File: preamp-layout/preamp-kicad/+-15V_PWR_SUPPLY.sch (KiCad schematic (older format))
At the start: 33 parts, among them J5 Screw_Terminal_01x03, J6 Conn_01x03_Male, J7 Conn_01x03_Male, J8 Conn_01x03_Male, T1 Transformer_1P_2S, U1 L7805, U2 LM7905_TO220

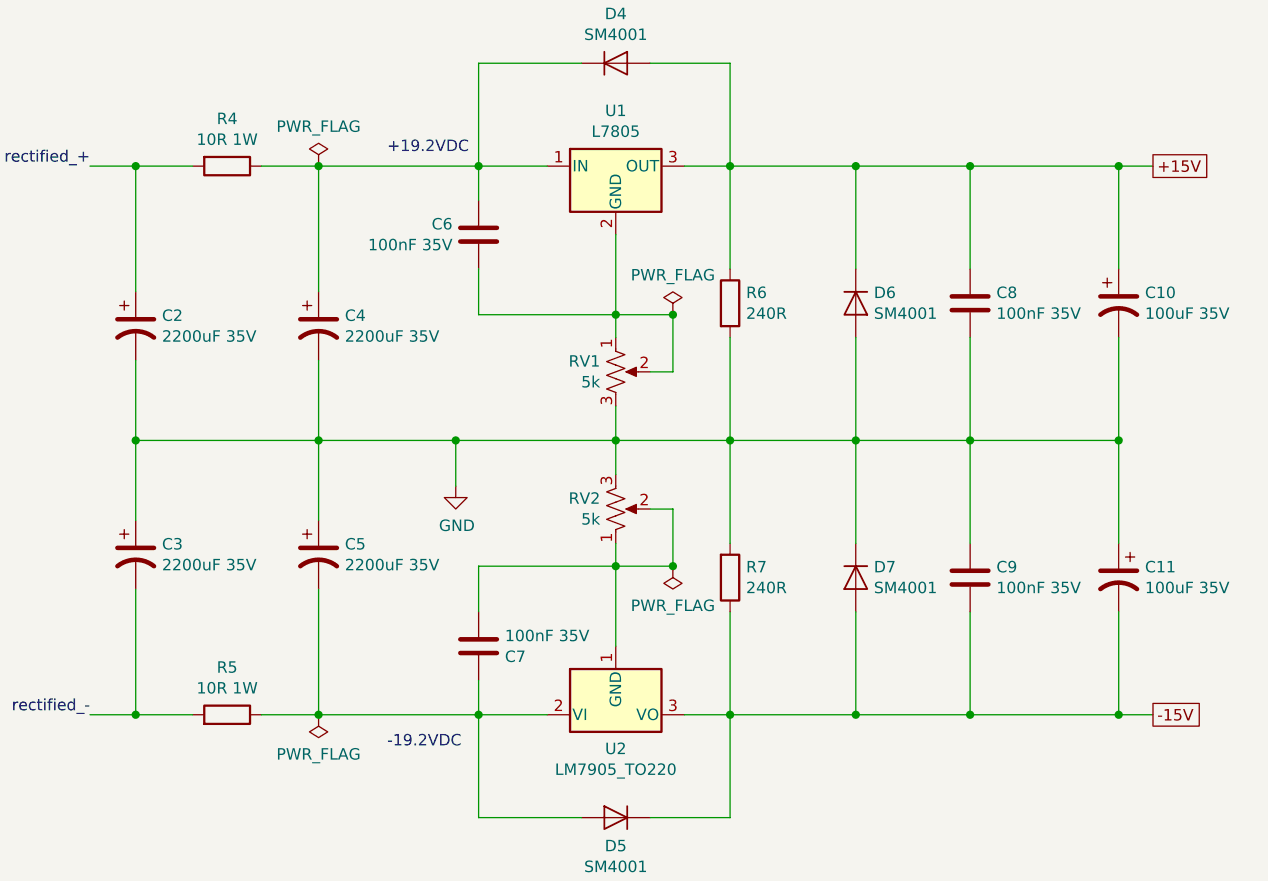
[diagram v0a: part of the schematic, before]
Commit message: Initial Review
Reviewing schematic, comparing to references and filling in BOM to match schematics. Updating footprints in the process as well.
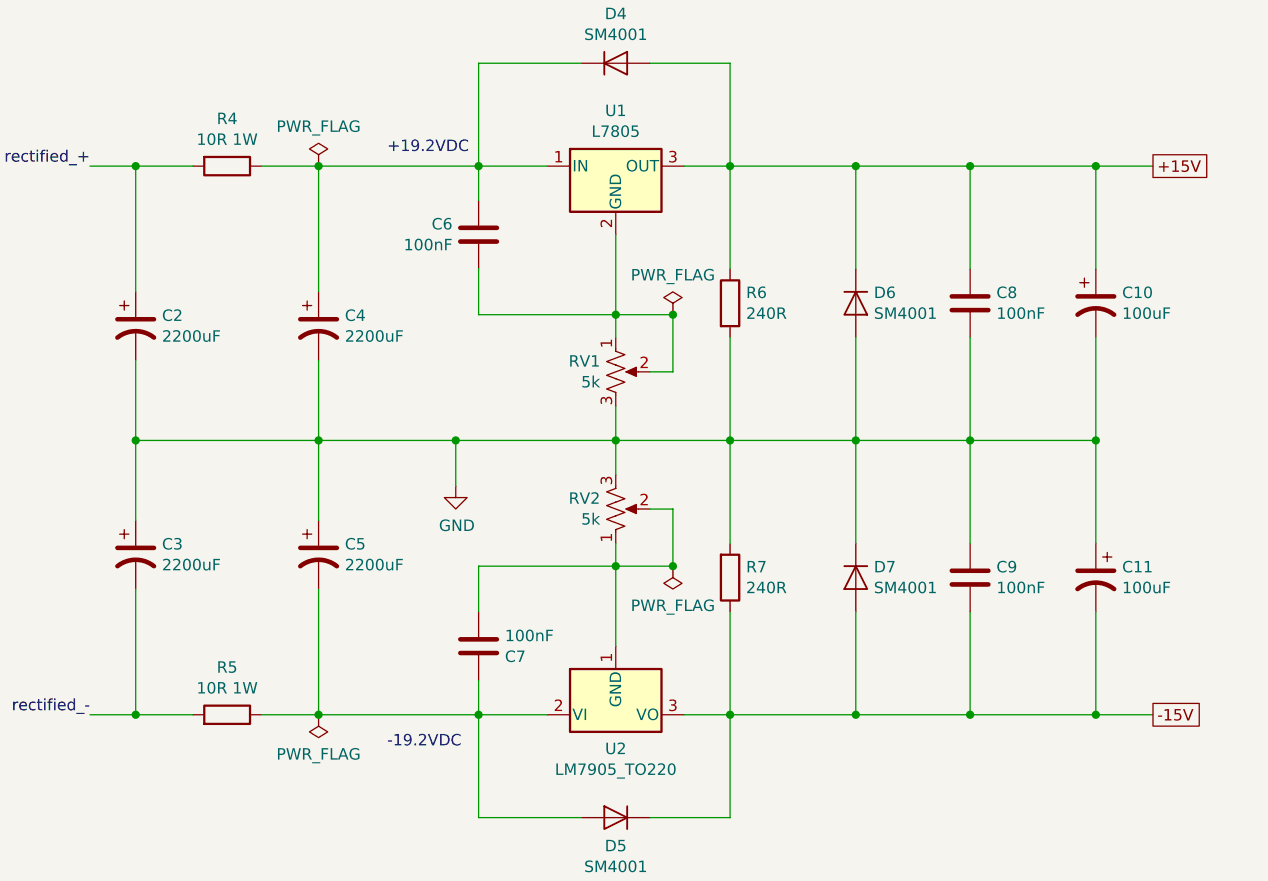
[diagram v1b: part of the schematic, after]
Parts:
- C10, C11: value 100uF 35V -> 100uF
- C2, C3, C4, C5: value 2200uF 35V -> 2200uF
- C6, C7, C8, C9: value 100nF 35V -> 100nF; footprint (none) -> Capacitor_SMD:C_0805_2012Metric_Pad1.15x1.40mm_HandSolder
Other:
- moved on the sheet: C10, C11
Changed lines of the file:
@@
 AR Path="/5E5EF2D4/5FE3F8A0" Ref="C?"  Part="1"
 F 0 "C8" H 9465 2996 50  0000 L CNN
-F 1 "100nF 35V" H 9465 2905 50  0000 L CNN
-F 2 "" H 9388 2800 50  0001 C CNN
+F 1 "100nF" H 9465 2905 50  0000 L CNN
+F 2 "Capacitor_SMD:C_0805_2012Metric_Pad1.15x1.40mm_HandSolder" H 9388 2800 50  0001 C CNN
 F 3 "~" H 9350 2950 50  0001 C CNN
 	1    9350 2950
@@
 AR Path="/5E5EF2D4/5FE3F8C5" Ref="C?"  Part="1"
 F 0 "C6" H 7086 2696 50  0000 R CNN
-F 1 "100nF 35V" H 7086 2605 50  0000 R CNN
-F 2 "" H 7238 2500 50  0001 C CNN
+F 1 "100nF" H 7086 2605 50  0000 R CNN
+F 2 "Capacitor_SMD:C_0805_2012Metric_Pad1.15x1.40mm_HandSolder" H 7238 2500 50  0001 C CNN
 F 3 "~" H 7200 2650 50  0001 C CNN
 	1    7200 2650
@@
 AR Path="/5E5EF2D4/5FE3F8CB" Ref="C?"  Part="1"
 F 0 "C2" H 5815 3096 50  0000 L CNN
-F 1 "2200uF 35V" H 5815 3005 50  0000 L CNN
+F 1 "2200uF" H 5815 3005 50  0000 L CNN
 F 2 "" H 5700 3050 50  0001 C CNN
 F 3 "~" H 5700 3050 50  0001 C CNN
@@
 AR Path="/5E5EF2D4/5FE3F8D1" Ref="C?"  Part="1"
 F 0 "C4" H 6615 3096 50  0000 L CNN
-F 1 "2200uF 35V" H 6615 3005 50  0000 L CNN
+F 1 "2200uF" H 6615 3005 50  0000 L CNN
 F 2 "" H 6500 3050 50  0001 C CNN
 F 3 "~" H 6500 3050 50  0001 C CNN
@@
 Connection ~ 9350 2350
 Wire Wire Line
-	10000 2800 10000 2350
-Connection ~ 10000 2350
-Wire Wire Line
-	10000 2350 10150 2350
+	9900 2800 9900 2350
 $Comp
 L Device:CP1 C?
 U 1 1 5FE3F8E7
-P 10000 2950
+P 9900 2950
 AR Path="/5FE3F8E7" Ref="C?"  Part="1"
 AR Path="/5E27B612/5FE3F8E7" Ref="C10"  Part="1"
 AR Path="/5E5EF2D4/5FE3F8E7" Ref="C?"  Part="1"
-F 0 "C10" H 10115 2996 50  0000 L CNN
-F 1 "100uF 35V" H 10115 2905 50  0000 L CNN
-F 2 "" H 10000 2950 50  0001 C CNN
-F 3 "~" H 10000 2950 50  0001 C CNN
-	1    10000 2950
-	1    0    0    -1
-$EndComp
-Wire Wire Line
-	10000 3100 10000 3550
+F 0 "C10" H 10015 2996 50  0000 L CNN
+F 1 "100uF" H 10015 2905 50  0000 L CNN
+F 2 "" H 9900 2950 50  0001 C CNN
+F 3 "~" H 9900 2950 50  0001 C CNN
+	1    9900 2950
+	1    0    0    -1
+$EndComp
+Wire Wire Line
+	9900 3100 9900 3550
 Text GLabel 10150 2350 2    50   UnSpc ~ 0
 +15V
@@
 Connection ~ 9350 3550
 Wire Wire Line
-	9350 3550 10000 3550
-Wire Wire Line
-	9350 2350 10000 2350
+	9350 3550 9900 3550
+Wire Wire Line
+	9350 2350 9900 2350
 Wire Wire Line
 	8850 2350 9350 2350
@@
 AR Path="/5E5EF2D4/5FE3F923" Ref="C?"  Part="1"
 F 0 "C9" H 9465 4104 50  0000 L CNN
-F 1 "100nF 35V" H 9465 4195 50  0000 L CNN
-F 2 "" H 9388 4000 50  0001 C CNN
+F 1 "100nF" H 9465 4195 50  0000 L CNN
+F 2 "Capacitor_SMD:C_0805_2012Metric_Pad1.15x1.40mm_HandSolder" H 9388 4000 50  0001 C CNN
 F 3 "~" H 9350 4150 50  0001 C CNN
 	1    9350 4150
@@
 AR Path="/5E5EF2D4/5FE3F948" Ref="C?"  Part="1"
 F 0 "C7" H 7315 4496 50  0000 L CNN
-F 1 "100nF 35V" H 7315 4405 50  0000 L CNN
-F 2 "" H 7238 4300 50  0001 C CNN
+F 1 "100nF" H 7315 4405 50  0000 L CNN
+F 2 "Capacitor_SMD:C_0805_2012Metric_Pad1.15x1.40mm_HandSolder" H 7238 4300 50  0001 C CNN
 F 3 "~" H 7200 4450 50  0001 C CNN
 	1    7200 4450
@@
 AR Path="/5E5EF2D4/5FE3F94E" Ref="C?"  Part="1"
 F 0 "C3" H 5815 4096 50  0000 L CNN
-F 1 "2200uF 35V" H 5815 4005 50  0000 L CNN
+F 1 "2200uF" H 5815 4005 50  0000 L CNN
 F 2 "" H 5700 4050 50  0001 C CNN
 F 3 "~" H 5700 4050 50  0001 C CNN
@@
 AR Path="/5E5EF2D4/5FE3F954" Ref="C?"  Part="1"
 F 0 "C5" H 6615 4096 50  0000 L CNN
-F 1 "2200uF 35V" H 6615 4005 50  0000 L CNN
+F 1 "2200uF" H 6615 4005 50  0000 L CNN
 F 2 "" H 6500 4050 50  0001 C CNN
 F 3 "~" H 6500 4050 50  0001 C CNN
@@
 Connection ~ 9350 4750
 Wire Wire Line
-	10000 4300 10000 4750
-Connection ~ 10000 4750
-Wire Wire Line
-	10000 4750 10150 4750
+	9900 4300 9900 4750
 $Comp
 L Device:CP1 C?
 U 1 1 5FE3F96A
-P 10000 4150
+P 9900 4150
 AR Path="/5FE3F96A" Ref="C?"  Part="1"
 AR Path="/5E27B612/5FE3F96A" Ref="C11"  Part="1"
 AR Path="/5E5EF2D4/5FE3F96A" Ref="C?"  Part="1"
-F 0 "C11" H 9885 4196 50  0000 R CNN
-F 1 "100uF 35V" H 9885 4105 50  0000 R CNN
-F 2 "" H 10000 4150 50  0001 C CNN
-F 3 "~" H 10000 4150 50  0001 C CNN
-	1    10000 4150
+F 0 "C11" H 9785 4196 50  0000 R CNN
+F 1 "100uF" H 9785 4105 50  0000 R CNN
+F 2 "" H 9900 4150 50  0001 C CNN
+F 3 "~" H 9900 4150 50  0001 C CNN
+	1    9900 4150
 	-1   0    0    -1
 $EndComp
 Wire Wire Line
-	10000 4000 10000 3550
+	9900 4000 9900 3550
 Text GLabel 10150 4750 2    50   UnSpc ~ 0
 -15V
@@
 	9350 4000 9350 3550
 Wire Wire Line
-	9350 4750 10000 4750
+	9350 4750 9900 4750
 Wire Wire Line
 	8850 4750 9350 4750
@@
 	0    -1   1    0
 $EndComp
-Connection ~ 10000 3550
 Wire Wire Line
 	7100 3550 7100 3750
@@
 Wire Wire Line
 	1550 3350 1950 3350
+Connection ~ 9900 2350
+Connection ~ 9900 3550
+Wire Wire Line
+	9900 2350 10150 2350
+Connection ~ 9900 4750
+Wire Wire Line
+	9900 4750 10150 4750
 $EndSCHEMATC

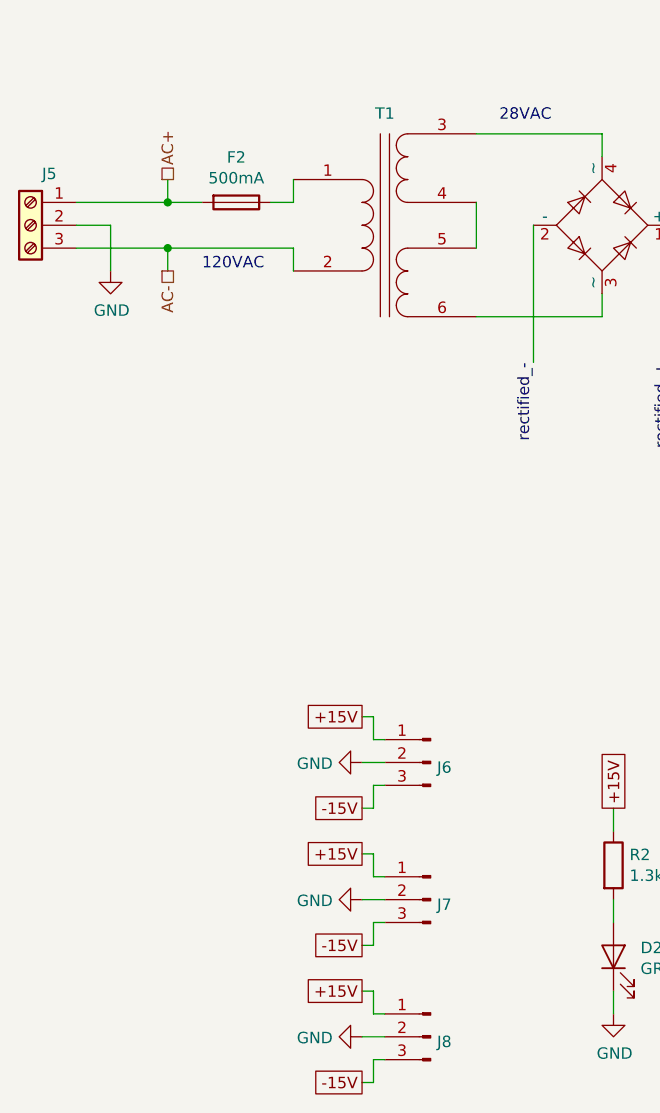
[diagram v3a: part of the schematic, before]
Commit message: BOM Update
parts added to BOM, connector cleanup. Stopping point before renumbering refdes in a more intelligent way.
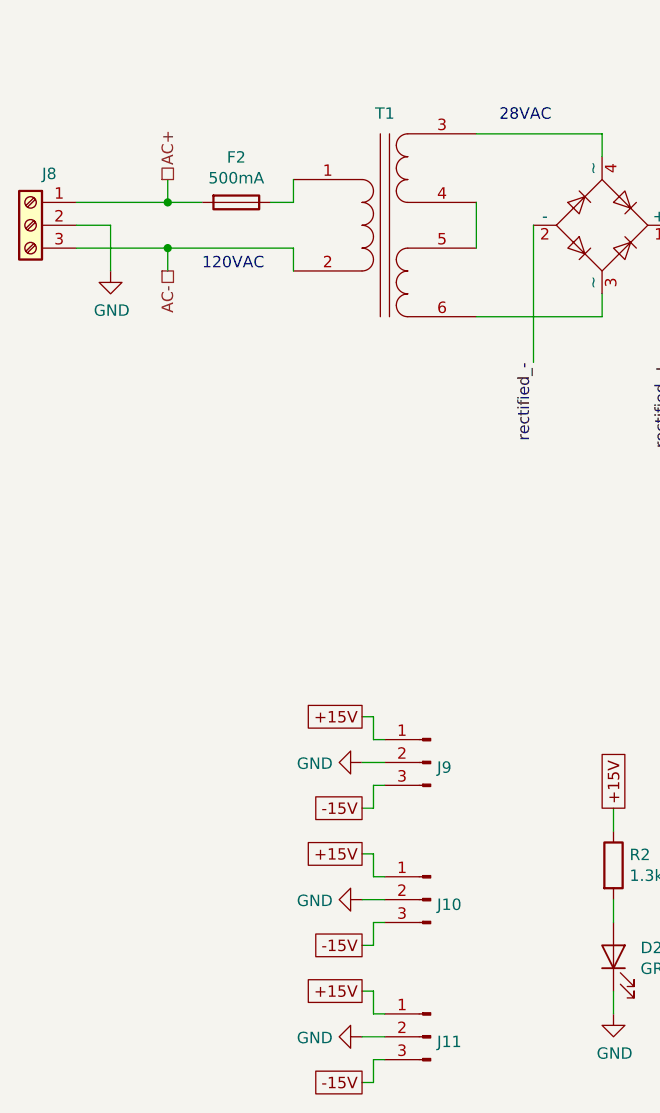
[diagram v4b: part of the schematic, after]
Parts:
- renumbered J7 to J10, J8 to J11, J5 to J8, J6 to J9
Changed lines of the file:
@@
 P 7100 3750
 AR Path="/5E26F6FE/649E59A9" Ref="#PWR?"  Part="1"
-AR Path="/5E27B612/649E59A9" Ref="#PWR09"  Part="1"
-F 0 "#PWR09" H 7100 3500 50  0001 C CNN
+AR Path="/5E27B612/649E59A9" Ref="#PWR012"  Part="1"
+F 0 "#PWR012" H 7100 3500 50  0001 C CNN
 F 1 "GND" H 7105 3577 50  0000 C CNN
 F 2 "" H 7100 3750 50  0001 C CNN
@@
 P 3900 6900
 AR Path="/5E26F6FE/649F2273" Ref="#PWR?"  Part="1"
-AR Path="/5E27B612/649F2273" Ref="#PWR07"  Part="1"
-F 0 "#PWR07" H 3900 6650 50  0001 C CNN
+AR Path="/5E27B612/649F2273" Ref="#PWR010"  Part="1"
+F 0 "#PWR010" H 3900 6650 50  0001 C CNN
 F 1 "GND" H 3905 6727 50  0000 C CNN
 F 2 "" H 3900 6900 50  0001 C CNN
@@
 P 4450 6900
 AR Path="/5E26F6FE/649FEF4E" Ref="#PWR?"  Part="1"
-AR Path="/5E27B612/649FEF4E" Ref="#PWR08"  Part="1"
-F 0 "#PWR08" H 4450 6650 50  0001 C CNN
+AR Path="/5E27B612/649FEF4E" Ref="#PWR011"  Part="1"
+F 0 "#PWR011" H 4450 6650 50  0001 C CNN
 F 1 "GND" H 4455 6727 50  0000 C CNN
 F 2 "" H 4450 6900 50  0001 C CNN
@@
 P 2800 7000
 AR Path="/5E26F6FE/64A0321E" Ref="#PWR?"  Part="1"
-AR Path="/5E27B612/64A0321E" Ref="#PWR06"  Part="1"
-F 0 "#PWR06" H 2800 6750 50  0001 C CNN
+AR Path="/5E27B612/64A0321E" Ref="#PWR09"  Part="1"
+F 0 "#PWR09" H 2800 6750 50  0001 C CNN
 F 1 "GND" V 2805 6872 50  0000 R CNN
 F 2 "" H 2800 7000 50  0001 C CNN
@@
 P 2800 6400
 AR Path="/5E26F6FE/64A1966F" Ref="#PWR?"  Part="1"
-AR Path="/5E27B612/64A1966F" Ref="#PWR05"  Part="1"
-F 0 "#PWR05" H 2800 6150 50  0001 C CNN
+AR Path="/5E27B612/64A1966F" Ref="#PWR08"  Part="1"
+F 0 "#PWR08" H 2800 6150 50  0001 C CNN
 F 1 "GND" V 2805 6272 50  0000 R CNN
 F 2 "" H 2800 6400 50  0001 C CNN
@@
 P 2800 5800
 AR Path="/5E26F6FE/64A1D9A5" Ref="#PWR?"  Part="1"
-AR Path="/5E27B612/64A1D9A5" Ref="#PWR04"  Part="1"
-F 0 "#PWR04" H 2800 5550 50  0001 C CNN
+AR Path="/5E27B612/64A1D9A5" Ref="#PWR07"  Part="1"
+F 0 "#PWR07" H 2800 5550 50  0001 C CNN
 F 1 "GND" V 2805 5672 50  0000 R CNN
 F 2 "" H 2800 5800 50  0001 C CNN
@@
 	4150 3450 4150 4050
 $Comp
-L Connector:Conn_01x03_Male J6
+L Connector:Conn_01x03_Male J9
 U 1 1 5E5A9FCF
 P 3100 5800
-AR Path="/5E27B612/5E5A9FCF" Ref="J6"  Part="1"
+AR Path="/5E27B612/5E5A9FCF" Ref="J9"  Part="1"
 AR Path="/6009D432/5E5A9FCF" Ref="J?"  Part="1"
 AR Path="/5E1A0CE1/5E5A9FCF" Ref="J?"  Part="1"
-F 0 "J6" H 3072 5778 50  0000 R CNN
+F 0 "J9" H 3072 5778 50  0000 R CNN
 F 1 "Conn_01x03_Male" H 3072 5733 50  0001 R CNN
 F 2 "Connector_JST:JST_EH_B3B-EH-A_1x03_P2.50mm_Vertical" H 3100 5800 50  0001 C CNN
@@
 $EndComp
 $Comp
-L Connector:Conn_01x03_Male J7
+L Connector:Conn_01x03_Male J10
 U 1 1 5E5BC88E
 P 3100 6400
-AR Path="/5E27B612/5E5BC88E" Ref="J7"  Part="1"
+AR Path="/5E27B612/5E5BC88E" Ref="J10"  Part="1"
 AR Path="/6009D432/5E5BC88E" Ref="J?"  Part="1"
 AR Path="/5E1A0CE1/5E5BC88E" Ref="J?"  Part="1"
-F 0 "J7" H 3072 6378 50  0000 R CNN
+F 0 "J10" H 3072 6378 50  0000 R CNN
 F 1 "Conn_01x03_Male" H 3072 6333 50  0001 R CNN
 F 2 "Connector_JST:JST_EH_B3B-EH-A_1x03_P2.50mm_Vertical" H 3100 6400 50  0001 C CNN
@@
 $EndComp
 $Comp
-L Connector:Conn_01x03_Male J8
+L Connector:Conn_01x03_Male J11
 U 1 1 5E5C1243
 P 3100 7000
-AR Path="/5E27B612/5E5C1243" Ref="J8"  Part="1"
+AR Path="/5E27B612/5E5C1243" Ref="J11"  Part="1"
 AR Path="/6009D432/5E5C1243" Ref="J?"  Part="1"
 AR Path="/5E1A0CE1/5E5C1243" Ref="J?"  Part="1"
-F 0 "J8" H 3072 6978 50  0000 R CNN
+F 0 "J11" H 3072 6978 50  0000 R CNN
 F 1 "Conn_01x03_Male" H 3072 6933 50  0001 R CNN
 F 2 "Connector_JST:JST_EH_B3B-EH-A_1x03_P2.50mm_Vertical" H 3100 7000 50  0001 C CNN
@@
 AR Path="/5E26F6FE/5E8FCAF8" Ref="J?"  Part="1"
 AR Path="/5E5EF2D4/5E8FCAF8" Ref="J?"  Part="1"
-AR Path="/5E27B612/5E8FCAF8" Ref="J5"  Part="1"
-F 0 "J5" H 1268 3675 50  0000 C CNN
+AR Path="/5E27B612/5E8FCAF8" Ref="J8"  Part="1"
+F 0 "J8" H 1268 3675 50  0000 C CNN
 F 1 "Screw_Terminal_01x03" H 1268 3216 50  0001 C CNN
 F 2 "TerminalBlock_Phoenix:TerminalBlock_Phoenix_MKDS-3-3-5.08_1x03_P5.08mm_Horizontal" H 1350 3450 50  0001 C CNN
@@
 P 1700 3650
 AR Path="/5E26F6FE/5E92CBD9" Ref="#PWR?"  Part="1"
-AR Path="/5E27B612/5E92CBD9" Ref="#PWR0112"  Part="1"
-F 0 "#PWR0112" H 1700 3400 50  0001 C CNN
+AR Path="/5E27B612/5E92CBD9" Ref="#PWR06"  Part="1"
+F 0 "#PWR06" H 1700 3400 50  0001 C CNN
 F 1 "GND" H 1705 3477 50  0000 C CNN
 F 2 "" H 1700 3650 50  0001 C CNN

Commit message: Schematic Redesignation
Regenerated RefDes for all parts, updated BOM accordingly and perfomred check on values, RefDes present from schematic to BOM. Value changes, BOM filled in as a result.
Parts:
- C6, C7, C8, C9: value 100nF -> 0.1uF
- U1: value L7805 -> LM7805
- U2: value LM7905_TO220 -> LM7905
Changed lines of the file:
@@
 AR Path="/5E5EF2D4/5FE3F8A0" Ref="C?"  Part="1"
 F 0 "C8" H 9465 2996 50  0000 L CNN
-F 1 "100nF" H 9465 2905 50  0000 L CNN
+F 1 "0.1uF" H 9465 2905 50  0000 L CNN
 F 2 "Capacitor_SMD:C_0805_2012Metric_Pad1.15x1.40mm_HandSolder" H 9388 2800 50  0001 C CNN
 F 3 "~" H 9350 2950 50  0001 C CNN
@@
 AR Path="/5E5EF2D4/5FE3F8C5" Ref="C?"  Part="1"
 F 0 "C6" H 7086 2696 50  0000 R CNN
-F 1 "100nF" H 7086 2605 50  0000 R CNN
+F 1 "0.1uF" H 7086 2605 50  0000 R CNN
 F 2 "Capacitor_SMD:C_0805_2012Metric_Pad1.15x1.40mm_HandSolder" H 7238 2500 50  0001 C CNN
 F 3 "~" H 7200 2650 50  0001 C CNN
@@
 AR Path="/5E27B612/5FE3F8F2" Ref="U1"  Part="1"
 F 0 "U1" H 7800 2592 50  0000 C CNN
-F 1 "L7805" H 7800 2501 50  0000 C CNN
+F 1 "LM7805" H 7800 2501 50  0000 C CNN
 F 2 "" H 7825 2200 50  0001 L CIN
 F 3 "http://www.st.com/content/ccc/resource/technical/document/datasheet/41/4f/b3/b0/12/d4/47/88/CD00000444.pdf/files/CD00000444.pdf/jcr:content/translations/en.CD00000444.pdf" H 7800 2300 50  0001 C CNN
@@
 AR Path="/5E27B612/5FE3F8FA" Ref="U2"  Part="1"
 F 0 "U2" H 7800 4601 50  0000 C CNN
-F 1 "LM7905_TO220" H 7800 4510 50  0000 C CNN
+F 1 "LM7905" H 7800 4510 50  0000 C CNN
 F 2 "Package_TO_SOT_THT:TO-220-3_Vertical" H 7800 4550 50  0001 C CIN
 F 3 "http://www.fairchildsemi.com/ds/LM/LM7905.pdf" H 7800 4750 50  0001 C CNN
@@
 AR Path="/5E5EF2D4/5FE3F923" Ref="C?"  Part="1"
 F 0 "C9" H 9465 4104 50  0000 L CNN
-F 1 "100nF" H 9465 4195 50  0000 L CNN
+F 1 "0.1uF" H 9465 4195 50  0000 L CNN
 F 2 "Capacitor_SMD:C_0805_2012Metric_Pad1.15x1.40mm_HandSolder" H 9388 4000 50  0001 C CNN
 F 3 "~" H 9350 4150 50  0001 C CNN
@@
 AR Path="/5E5EF2D4/5FE3F948" Ref="C?"  Part="1"
 F 0 "C7" H 7315 4496 50  0000 L CNN
-F 1 "100nF" H 7315 4405 50  0000 L CNN
+F 1 "0.1uF" H 7315 4405 50  0000 L CNN
 F 2 "Capacitor_SMD:C_0805_2012Metric_Pad1.15x1.40mm_HandSolder" H 7238 4300 50  0001 C CNN
 F 3 "~" H 7200 4450 50  0001 C CNN
